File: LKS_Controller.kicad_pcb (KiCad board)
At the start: 2 copper layers, 43 x 37 mm, 44 parts, among them J1 Conn_02x05_Odd_Even, Q1 IRLZ44N, Q2 IRLZ44N, Q3 IRLZ44N, Q4 IRLZ44N, Q5 IRLZ44N, Q6 IRLZ44N

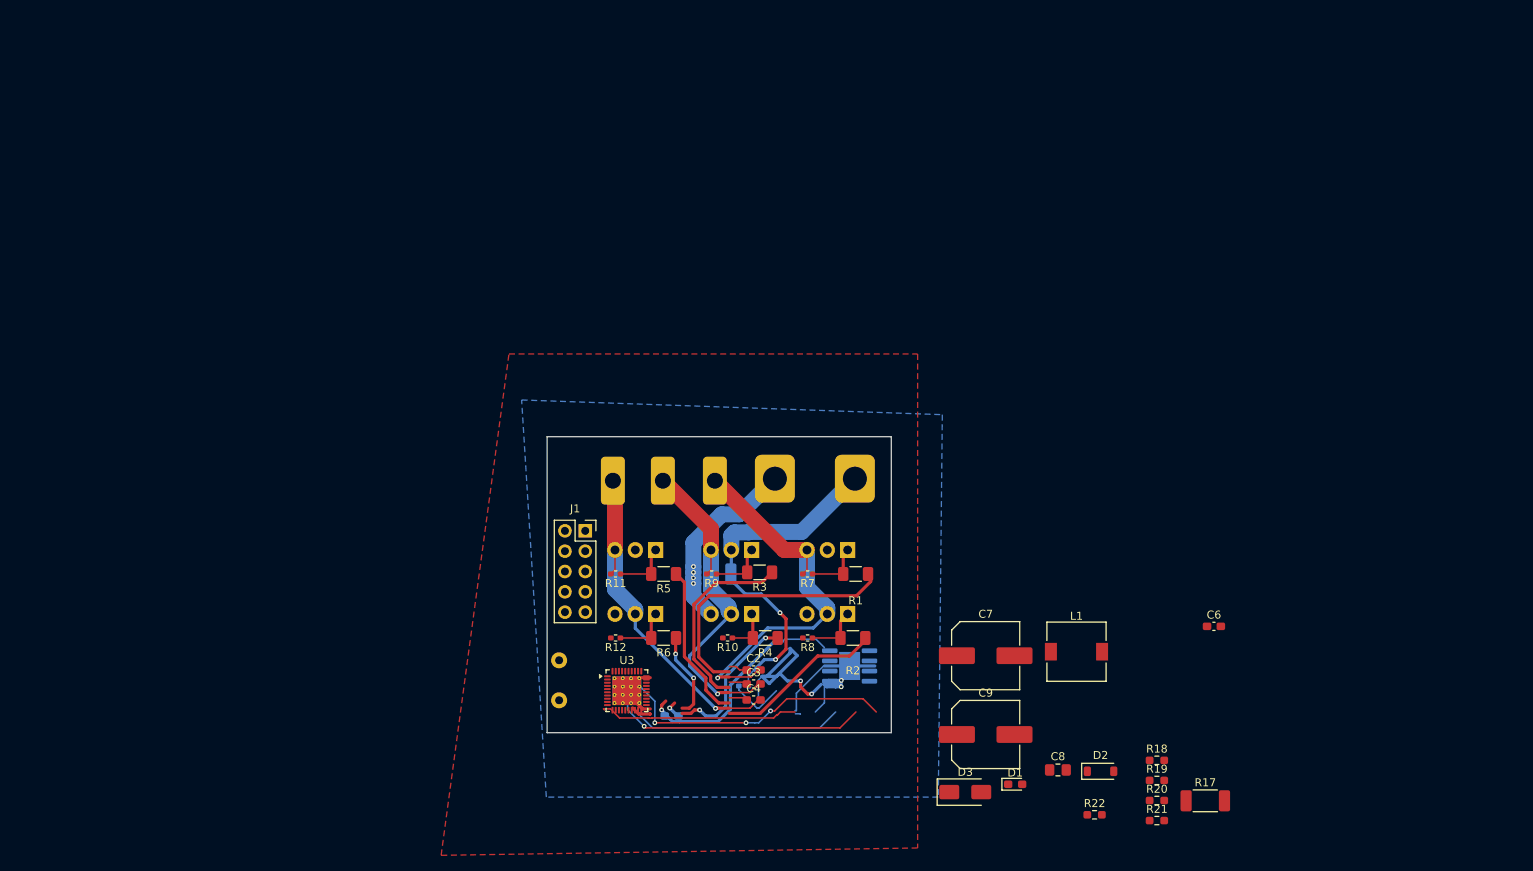
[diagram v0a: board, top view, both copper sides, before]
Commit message: updated layout, power supply schematic
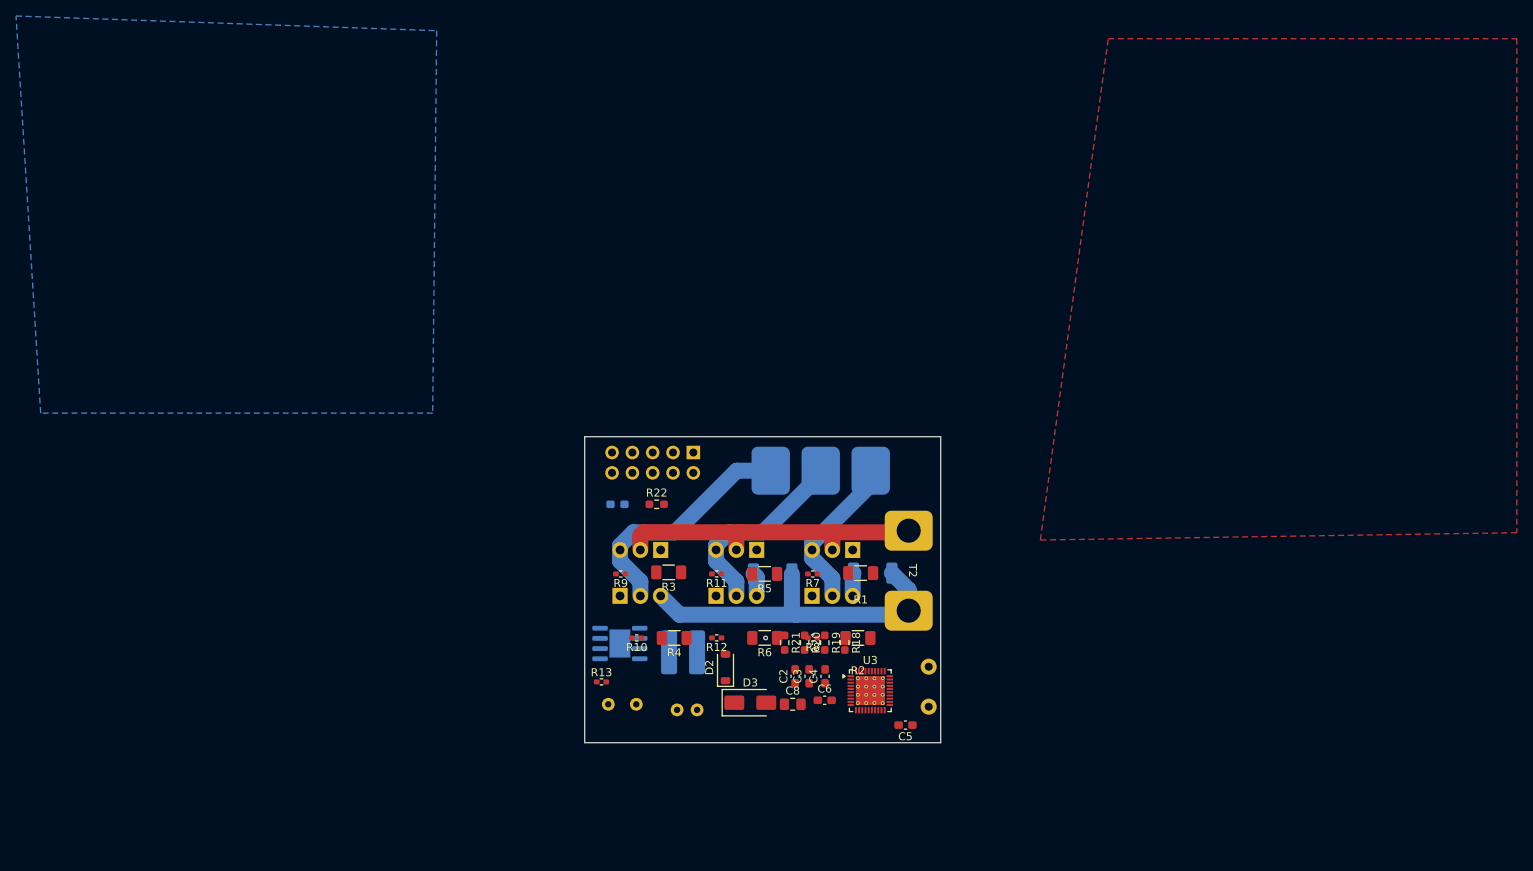
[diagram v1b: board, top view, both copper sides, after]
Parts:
- C5, R13, T2: moved to F.Cu
- C7: footprint Capacitor_SMD:C_Elec_8x10.2 -> Capacitor_THT:C_Radial_D6.3mm_H11.0mm_P2.50mm; moved to B.Cu
- C9: footprint Capacitor_SMD:C_Elec_8x10.2 -> Capacitor_THT:C_Radial_D8.0mm_H11.5mm_P3.50mm; moved to B.Cu
- D1, J1, R17: moved to B.Cu
- L1: value 47uH -> 100uH; footprint Inductor_SMD:L_7.3x7.3_H4.5 -> Vesc_footprints:100uH inductor 5x5mm; moved to B.Cu
- moved R22 67.1 mm to (110.5, 100.2)
- moved R17 61.1 mm to (125.0, 108.9)
- moved D1 60.8 mm to (105.6, 100.2), turned to 180 degrees
- moved R21 51.6 mm to (126.5, 117.5), turned to -90 degrees
- moved C6 49.5 mm to (131.5, 124.7)
- moved L1 49.2 mm to (113.8, 118.7), turned to 180 degrees
- moved D2 48.6 mm to (119.1, 120.6), turned to 90 degrees
- moved R20 48.2 mm to (129.0, 117.5), turned to -90 degrees
- moved C1 45.7 mm to (144.0, 123.0), turned to -90 degrees
- moved R19 44.9 mm to (131.5, 117.5), turned to -90 degrees
- moved C9 43.8 mm to (108.0, 125.2), turned to 180 degrees
- moved R18 41.7 mm to (134.0, 117.5), turned to -90 degrees
- moved C7 36.7 mm to (115.5, 125.9), turned to 180 degrees
- moved C8 34.2 mm to (127.5, 125.2)
- moved U3 30.4 mm to (137.2, 123.5)
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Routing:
- net (no net): track 146.3 -> 0.00 mm, vias 4 -> 0
- net GHA: track 34.8 -> 0.00 mm
- net G_VDD: track 31.0 -> 0.00 mm, vias 1 -> 0
- net SHA: track 49.9 -> 19.7 mm, vias 1 -> 0
- net GHB: track 24.5 -> 0.00 mm
- net GLA: track 21.1 -> 0.00 mm
- net GHC: track 19.7 -> 0.00 mm
- net GLB: track 18.6 -> 0.00 mm, vias 2 -> 0
- net -BATT: track 61.5 -> 43.4 mm, vias 9 -> 0
- net SHB: track 42.6 -> 24.6 mm, vias 1 -> 0
- net SHC: track 43.1 -> 30.0 mm, vias 1 -> 0
- net GLC: track 10.9 -> 0.00 mm, vias 2 -> 1
- net Net-(Q4-G): track 7.08 -> 0.00 mm
- net Net-(Q3-G): track 7.08 -> 0.00 mm
- net Net-(Q1-G): track 7.08 -> 0.00 mm
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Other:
- board size 43 x 37 mm -> 44.5 x 38.2 mm

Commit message: started routing
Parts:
- R18, R19, R20, R21: moved to B.Cu
- moved R6 17.9 mm to (106.2, 116.5), turned to 0 degrees
- moved R10 15.0 mm to (123.0, 116.6), turned to 0 degrees
- moved R21 12.2 mm to (128.4, 129.5), turned to 0 degrees
- moved R3 12.0 mm to (124.0, 108.9)
- moved R5 12.0 mm to (112.0, 108.7)
- moved R11 12.0 mm to (106.0, 108.9)
- moved R9 12.0 mm to (118.0, 108.9)
- moved R18 10.8 mm to (132.4, 128.2), turned to 0 degrees
- moved C6 10.5 mm to (141.7, 127.1)
- moved R20 10.2 mm to (128.2, 127.7), turned to 0 degrees
- moved R19 8.94 mm to (132.4, 126.4), turned to 0 degrees
- moved R12 7.16 mm to (110.8, 116.5), turned to 0 degrees
- moved C2 6.96 mm to (134.5, 119.8), turned to 135 degrees
- moved C8 5.98 mm to (122.0, 122.8)
- moved R2 5.76 mm to (129.9, 116.5), turned to 0 degrees
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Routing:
- net SHB: track 24.6 -> 60.0 mm, vias 0 -> 1
- net GHC: track 0.00 -> 31.0 mm
- net SHC: track 30.0 -> 60.4 mm, vias 0 -> 1
- net GLC: track 0.00 -> 26.2 mm, vias 1 -> 0
- net GHB: track 0.00 -> 21.2 mm
- net SHA: track 19.7 -> 39.3 mm, vias 0 -> 1
- net GHA: track 0.00 -> 16.7 mm
- net GLB: track 0.00 -> 15.8 mm
- net Net-(Q4-G): track 0.00 -> 9.05 mm
- net Net-(Q2-G): track 0.00 -> 8.97 mm
- net Net-(Q6-G): track 0.00 -> 8.16 mm
- net Net-(Q3-G): track 0.00 -> 7.08 mm
- net Net-(Q1-G): track 0.00 -> 7.02 mm
- net Net-(Q5-G): track 0.00 -> 6.96 mm
- net Net-(Q2-S): track 2.89 -> 8.20 mm
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
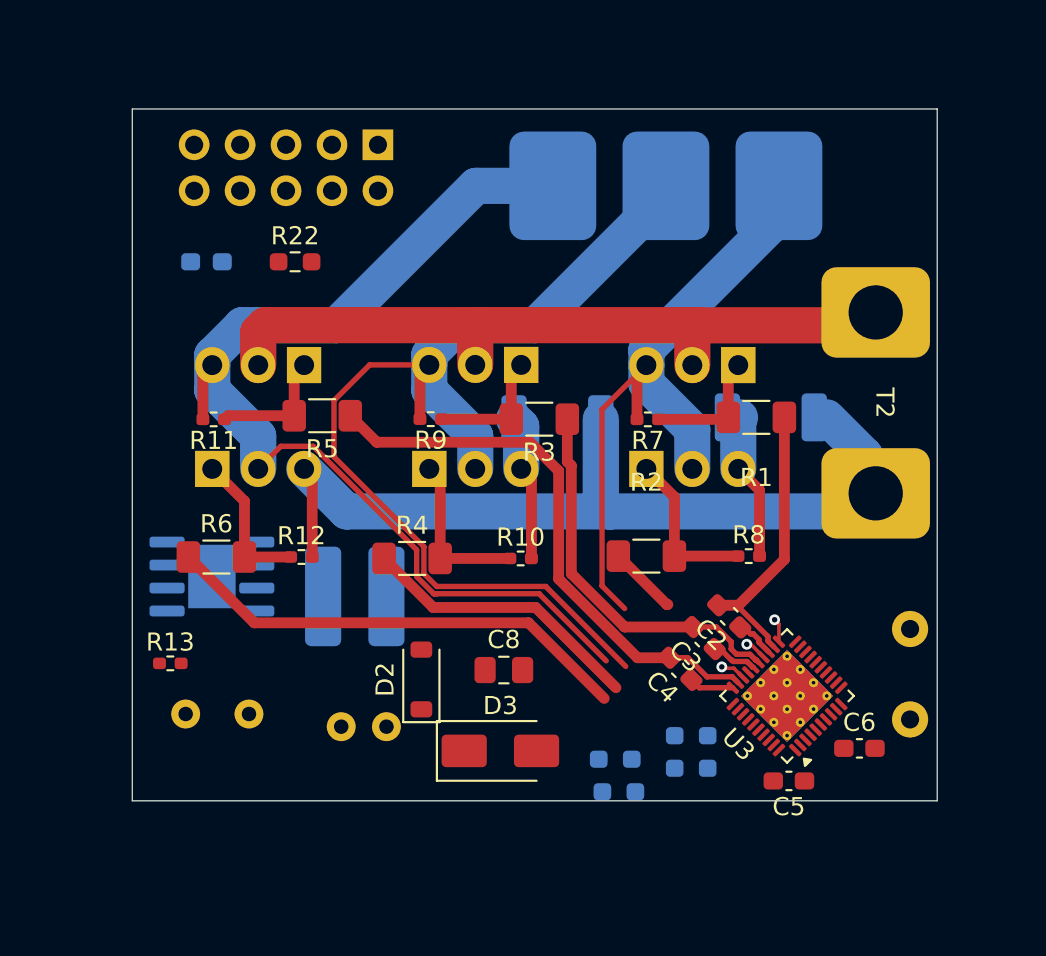
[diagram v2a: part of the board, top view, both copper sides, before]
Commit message: Fix ESC power, gate drive and current sensing schematics
Correct the buck converter and MCU symbols, bootstrap networks, MOSFET pulldowns and current sensing components. Migrate project libraries, synchronize PCB footprints and ground nets, and resolve ERC errors and warnings. Include LCSC BOMs and design notes; PCB routing remains incomplete.
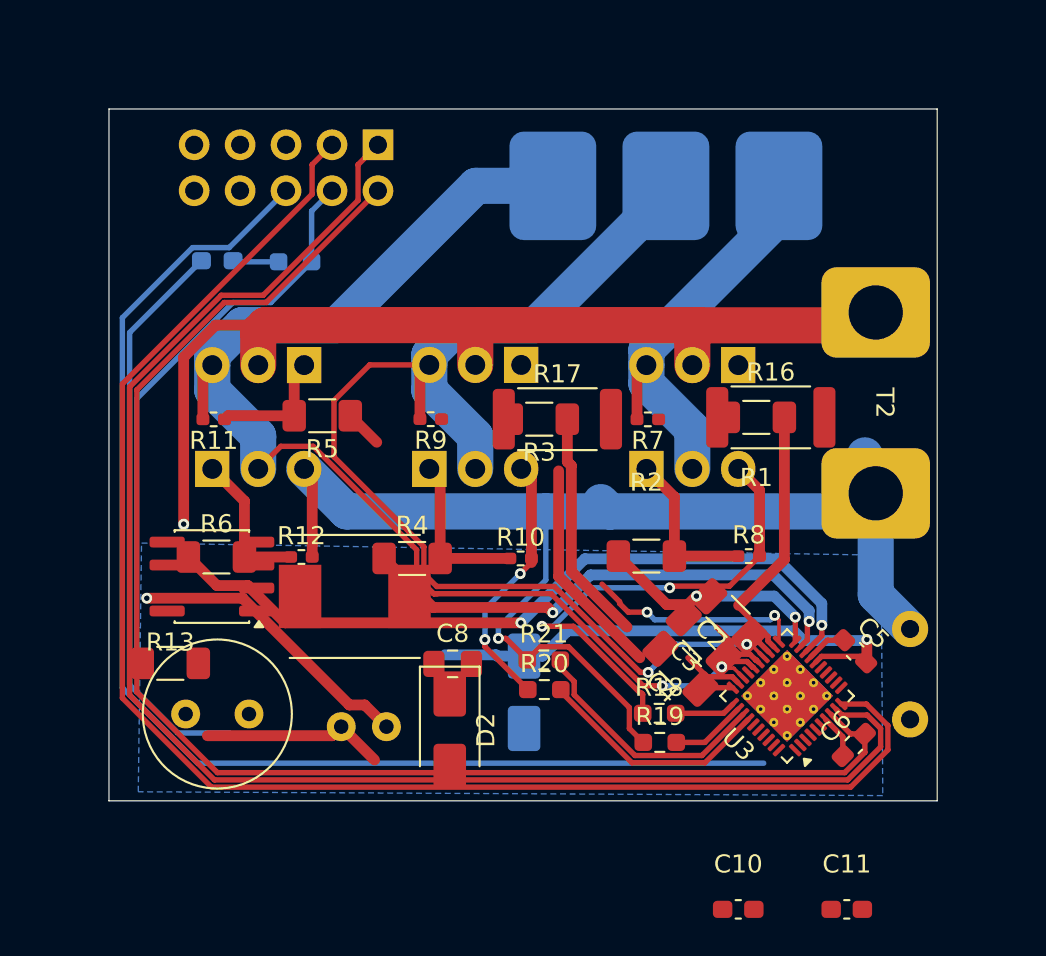
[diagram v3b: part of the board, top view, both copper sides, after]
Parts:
- added C10: 1nF 50V C0G, Capacitor_SMD:C_0603_1608Metric_Pad1.08x0.95mm_HandSolder, F.Cu at (135.0, 136.0)
- added C11: 1nF 50V C0G, Capacitor_SMD:C_0603_1608Metric_Pad1.08x0.95mm_HandSolder, F.Cu at (141.0, 136.0)
- C1: footprint Vesc_footprints:Capacitor_50v_1000uf -> Custom_footprints:C_Radial_P5mm_AsRouted
- C2, C3, C4: value C_Small -> 4.7uF; footprint Capacitor_SMD:C_0603_1608Metric_Pad1.08x0.95mm_HandSolder -> Capacitor_SMD:C_1206_3216Metric_Pad1.33x1.80mm_HandSolder
- C7: value 10uF 160v -> 10uF 100V
- C8: value 2.2nF -> 1uF 50V X7R
- C9: value 470uF 16v -> 470uF 25V; footprint Capacitor_THT:C_Radial_D8.0mm_H11.5mm_P3.50mm -> Custom_footprints:C_Radial_D8.0mm_H12.0mm_P3.50mm; moved to F.Cu
- D1: value LED -> Green LED
- D2: value MBR0540 -> SS310; footprint Diode_SMD:D_SOD-123 -> Diode_SMD:D_SMA
- D3: value SMAJ5.0A -> M7; moved to B.Cu
- L1: value 100uH -> 100uH 1.5A Isat2A; footprint Vesc_footprints:100uH inductor 5x5mm -> Custom_footprints:L_XR_XR0650; moved to F.Cu
- R10, R11, R12, R9: value 100 -> 10k
- R13: value 50k -> 0.5R 1% 0.5W; footprint Resistor_SMD:R_0402_1005Metric_Pad0.72x0.64mm_HandSolder -> Resistor_SMD:R_1206_3216Metric_Pad1.30x1.75mm_HandSolder
- R16, R17: value R -> 1mR 1% 3W; footprint Resistor_SMD:R_2010_5025Metric_Pad1.40x2.65mm_HandSolder -> Resistor_SMD:R_2512_6332Metric; moved to F.Cu
- R18, R19, R20, R21: value R_Small -> 100R 1%; moved to F.Cu
- R22: value R_Small -> 4.7k 1%; moved to B.Cu
- R7, R8: value 100k -> 10k
- T1: footprint Vesc_footprints:ABC_Terminal -> Custom_footprints:ABC_Terminal
- T2: footprint Vesc_footprints:Untitled -> Custom_footprints:Battery_Wire_Pads_P10mm
- U2: value ~ -> U3212; footprint Package_SO:SOIC-8-1EP_3.9x4.9mm_P1.27mm_EP2.62x3.51mm -> Custom_footprints:U3212_SOP-7_3.9x4.9mm_P1.27mm; moved to F.Cu
- U3: value ~ -> LKS32MC034SF6Q8
- moved R21 8.39 mm to (124.2, 122.2)
- moved C5 8.05 mm to (141.5, 121.7), turned to -45 degrees
- moved R20 5.49 mm to (124.3, 123.8)
- moved R18 3.52 mm to (130.6, 125.2)
- moved D3 3.49 mm to (123.2, 124.0), turned to 90 degrees
- moved D2 3.21 mm to (119.0, 126.1), turned to -90 degrees
- moved C8 2.85 mm to (119.2, 122.4)
- moved R19 1.78 mm to (130.7, 126.8)
- moved D1 0.60 mm to (106.2, 100.1)
- moved C6 0.36 mm to (141.4, 126.9), turned to 45 degrees
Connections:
- net Net-(D3-A1) renamed /Power_Supply/BUCK_VDD
- C2 pad 2: GHA -> SHA
- C3 pad 2: GHB -> SHB
- C4 pad 2: GHC -> SHC
- C5 pad 1: GND -> -BATT
- C6 pad 1: Net-(J1-Pin_5) -> -BATT
- C7 pad 2: GND -> -BATT
- C8 pad 1: Net-(D2-K) -> /Power_Supply/BUCK_SW
- C9 pad 2: GND -> -BATT
- D2 pad 1: Net-(D2-K) -> /Power_Supply/BUCK_SW
- D2 pad 2: GND -> -BATT
- J1 pad 4: GND -> -BATT
- J1 pad 5: Net-(J1-Pin_5) -> -BATT
- L1 pad 1: Net-(D2-K) -> /Power_Supply/BUCK_SW
- R13 pad 2: Net-(D2-K) -> /Power_Supply/BUCK_SW
- R22 pad 2: GND -> -BATT
- U2 pad 2: Net-(D2-K) -> /Power_Supply/BUCK_SW
- U2 pad 5: Net-(D2-K) -> +BATT
- U2 pad 8: +BATT -> unconnected-(U2-NC-Pad8)
- U3 pad 13: GND -> -BATT
- U3 pad 17: GND -> -BATT
- U3 pad 41: (no net) -> -BATT
- U3 pad 7: Net-(J1-Pin_5) -> -BATT
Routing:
- net Net-(J1-Pin_1): track 0.00 -> 85.6 mm
- net Net-(J1-Pin_3): track 0.00 -> 85.0 mm
- net Net-(J1-Pin_2): track 0.00 -> 80.5 mm
- net Net-(J1-Pin_6): track 0.00 -> 69.6 mm
- net -BATT: track 48.4 -> 115.7 mm, vias 0 -> 1
- net G_VDD: track 0.00 -> 60.3 mm, vias 0 -> 1
- net +BATT: track 40.8 -> 71.5 mm, vias 0 -> 2
- net Net-(Q2-S): track 8.20 -> 27.1 mm, vias 0 -> 2
- net GLC: track 26.2 -> 42.1 mm, vias 0 -> 2
- net OPA1_IN: track 0.00 -> 13.9 mm
- net GHC: track 31.0 -> 17.6 mm
- net OPA1_IP: track 0.00 -> 13.1 mm
- net GLB: track 15.8 -> 28.6 mm, vias 0 -> 2
- net GLA: track 3.85 -> 12.9 mm, vias 0 -> 2
- net SHB: track 60.0 -> 67.5 mm, vias 1 -> 2
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- added copper zone on B.Cu, net -BATT
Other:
- board size 44.5 x 38.2 mm -> 45.8 x 38.2 mm
